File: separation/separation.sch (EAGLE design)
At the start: 9 parts, among them IC1 L7805ACV

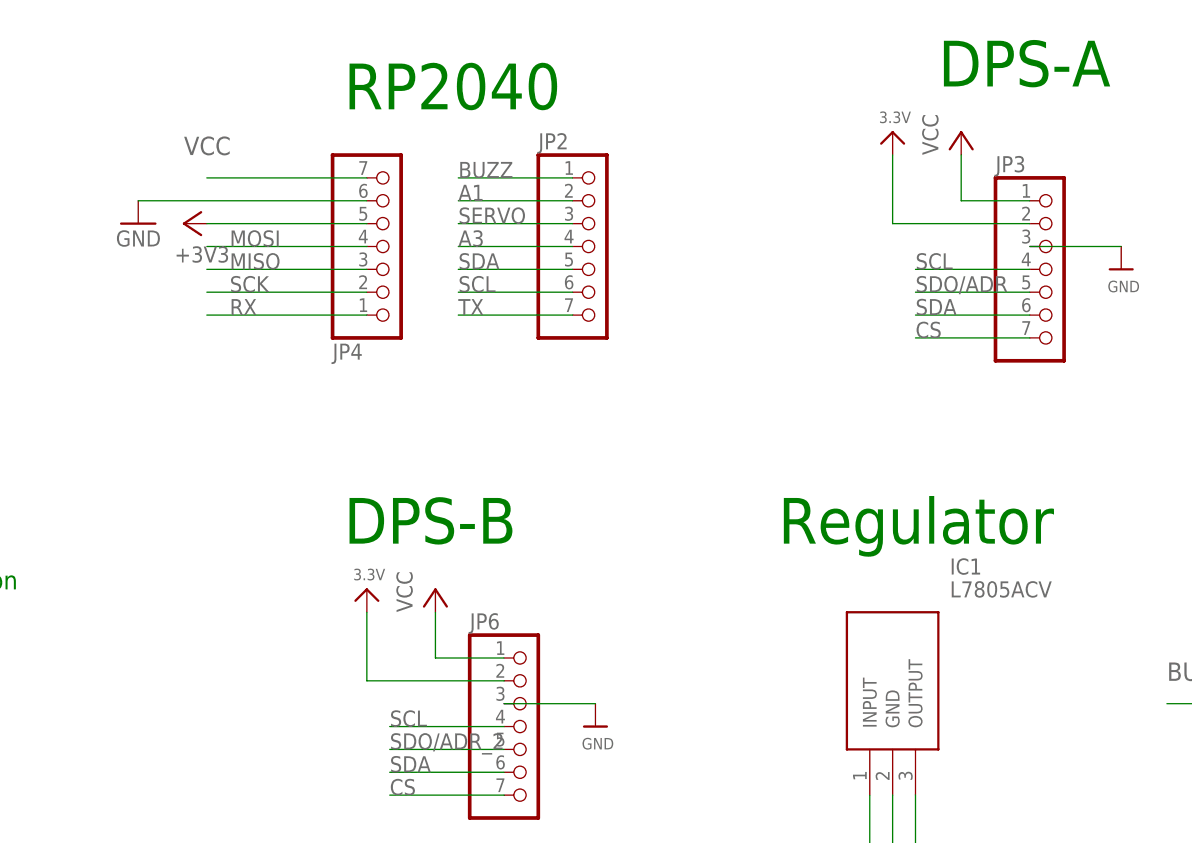
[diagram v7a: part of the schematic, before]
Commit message: remove all 3v3 lines
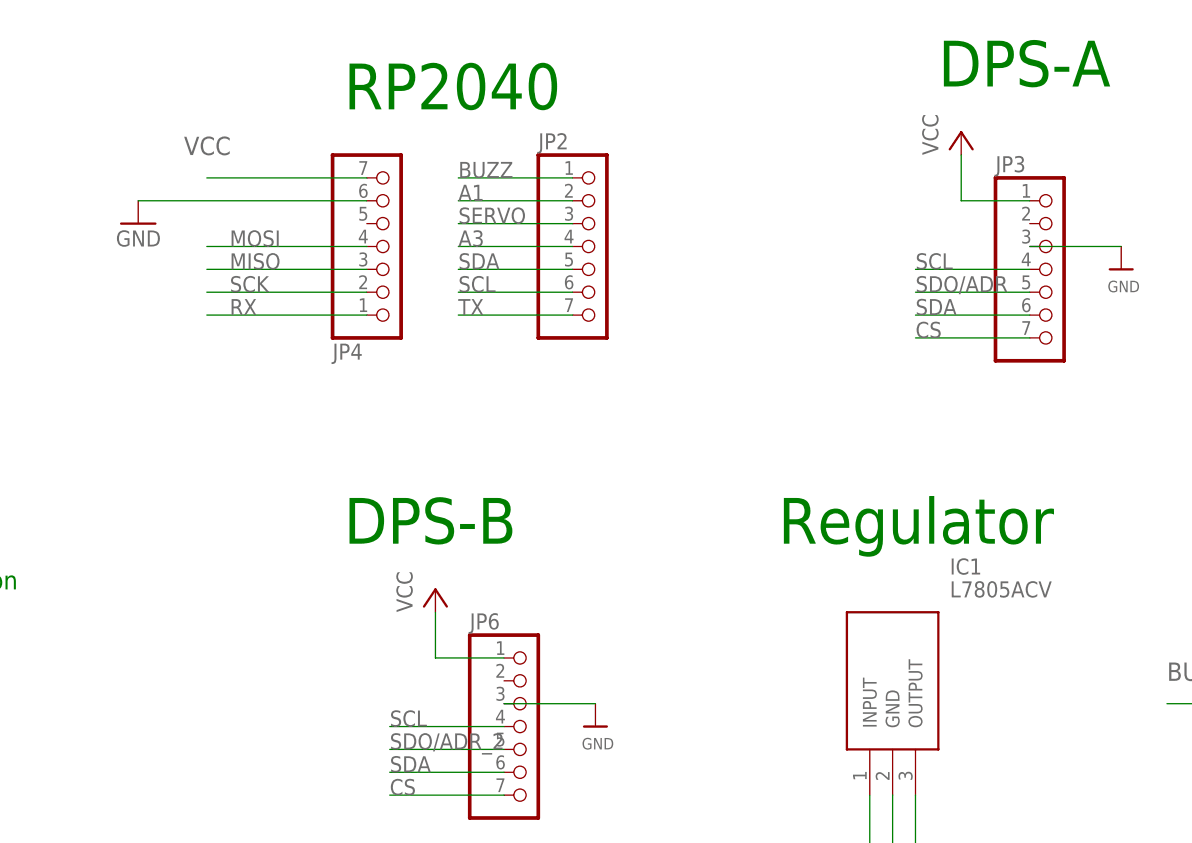
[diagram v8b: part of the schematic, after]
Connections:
- removed net +3V3: JP4.5
- removed net 3.3V: JP3.2, JP6.2
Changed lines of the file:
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@@
 <part name="GND1" library="supply1" library_urn="urn:adsk.eagle:library:371" deviceset="GND" device=""/>
 <part name="JP4" library="microbuilder" deviceset="HEADER-1X7" device=""/>
-<part name="+3V1" library="supply1" library_urn="urn:adsk.eagle:library:371" deviceset="+3V3" device=""/>
 <part name="U$1" library="microbuilder" deviceset="GND" device=""/>
-<part name="U$2" library="microbuilder" deviceset="3.3V" device=""/>
 <part name="P+1" library="supply1" library_urn="urn:adsk.eagle:library:371" deviceset="VCC" device=""/>
 <part name="JP3" library="microbuilder" deviceset="HEADER-1X7" device="70MIL"/>
 <part name="U$5" library="microbuilder" deviceset="GND" device=""/>
-<part name="U$6" library="microbuilder" deviceset="3.3V" device=""/>
 <part name="P+3" library="supply1" library_urn="urn:adsk.eagle:library:371" deviceset="VCC" device=""/>
 <part name="JP6" library="microbuilder" deviceset="HEADER-1X7" device="70MIL"/>
@@
 <attribute name="VALUE" x="29.21" y="76.2" size="1.778" layer="96" rot="MR180"/>
 </instance>
-<instance part="+3V1" gate="G$1" x="12.7" y="66.04" smashed="yes" rot="R90">
-<attribute name="VALUE" x="17.78" y="63.5" size="1.778" layer="96" rot="R180"/>
-</instance>
 <instance part="U$1" gate="G$1" x="116.84" y="60.96" smashed="yes">
 <attribute name="VALUE" x="115.316" y="58.42" size="1.27" layer="96"/>
-</instance>
-<instance part="U$2" gate="G$1" x="91.44" y="76.2" smashed="yes">
-<attribute name="VALUE" x="89.916" y="77.216" size="1.27" layer="96"/>
 </instance>
 <instance part="P+1" gate="VCC" x="99.06" y="76.2" smashed="yes">
@@
 <instance part="U$5" gate="G$1" x="58.42" y="10.16" smashed="yes">
 <attribute name="VALUE" x="56.896" y="7.62" size="1.27" layer="96"/>
-</instance>
-<instance part="U$6" gate="G$1" x="33.02" y="25.4" smashed="yes">
-<attribute name="VALUE" x="31.496" y="26.416" size="1.27" layer="96"/>
 </instance>
 <instance part="P+3" gate="VCC" x="40.64" y="25.4" smashed="yes">
@@
 </segment>
 </net>
-<net name="+3V3" class="0">
-<segment>
-<wire x1="33.02" y1="66.04" x2="15.24" y2="66.04" width="0.1524" layer="91"/>
-<pinref part="JP4" gate="A" pin="5"/>
-<pinref part="+3V1" gate="G$1" pin="+3V3"/>
-</segment>
-</net>
 <net name="SCL" class="0">
 <segment>
@@
 </segment>
 </net>
-<net name="3.3V" class="2">
-<segment>
-<wire x1="106.68" y1="66.04" x2="91.44" y2="66.04" width="0.1524" layer="91"/>
-<wire x1="91.44" y1="66.04" x2="91.44" y2="73.66" width="0.1524" layer="91"/>
-<pinref part="U$2" gate="G$1" pin="3.3V"/>
-<pinref part="JP3" gate="A" pin="2"/>
-</segment>
-<segment>
-<wire x1="48.26" y1="15.24" x2="33.02" y2="15.24" width="0.1524" layer="91"/>
-<wire x1="33.02" y1="15.24" x2="33.02" y2="22.86" width="0.1524" layer="91"/>
-<pinref part="U$6" gate="G$1" pin="3.3V"/>
-<pinref part="JP6" gate="A" pin="2"/>
-</segment>
-</net>
